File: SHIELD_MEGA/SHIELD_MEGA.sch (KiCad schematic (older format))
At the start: 2 parts

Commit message: Updating main sheet
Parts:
- added C1, C2, C3, C4: 100n, symbol Device:C
- gave numbers to parts that had none: 2
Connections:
- net +3V3: now also C1.1, C2.1
- net +5V: now also C3.1, C4.1
- net GND: now also C1.2, C2.2, C3.2, C4.2
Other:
- moved on the sheet: J1
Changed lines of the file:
@@
 $Descr A4 11693 8268
 encoding utf-8
-Sheet 1 9
-Title ""
-Date ""
-Rev ""
-Comp ""
+Sheet 1 10
+Title "SHIELD ARDUINO MEGA"
+Date "2021-11-21"
+Rev "V1"
+Comp "PROEX - UNIFEI"
 Comment1 ""
 Comment2 ""
 Comment3 ""
-Comment4 ""
+Comment4 "LINCOLN WALLACE VELOSO ALMEIDA"
 $EndDescr
 $Comp
-L Connector:Conn_01x03_Male J?
+L Connector:Conn_01x03_Male J2
 U 1 1 61954CC1
 P 9750 5950
-F 0 "J?" H 9800 6200 50  0000 C CNN
+F 0 "J2" H 9800 6200 50  0000 C CNN
 F 1 "Conn_01x03_Male" V 9700 5950 50  0000 C CNN
 F 2 "" H 9750 5950 50  0001 C CNN
@@
 $EndComp
 $Comp
-L power:+3.3V #PWR?
+L power:+3.3V #PWR01
 U 1 1 6195629E
 P 10050 5850
-F 0 "#PWR?" H 10050 5700 50  0001 C CNN
+F 0 "#PWR01" H 10050 5700 50  0001 C CNN
 F 1 "+3.3V" V 10065 5978 50  0000 L CNN
 F 2 "" H 10050 5850 50  0001 C CNN
@@
 $EndComp
 $Comp
-L power:+5V #PWR?
+L power:+5V #PWR03
 U 1 1 61956DDE
 P 10700 5950
-F 0 "#PWR?" H 10700 5800 50  0001 C CNN
+F 0 "#PWR03" H 10700 5800 50  0001 C CNN
 F 1 "+5V" V 10715 6078 50  0000 L CNN
 F 2 "" H 10700 5950 50  0001 C CNN
@@
 $EndComp
 $Comp
-L power:GND #PWR?
+L power:GND #PWR02
 U 1 1 6195741C
 P 10050 6050
-F 0 "#PWR?" H 10050 5800 50  0001 C CNN
+F 0 "#PWR02" H 10050 5800 50  0001 C CNN
 F 1 "GND" V 10055 5922 50  0000 R CNN
 F 2 "" H 10050 6050 50  0001 C CNN
@@
 Wire Wire Line
 	3400 2450 3300 2450
-Text HLabel 8300 1250 2    50   Input ~ 0
-GND
 $Sheet
 S 8300 1050 1200 1600
@@
 F0 "ESCs" 50
 F1 "ESC_PWMs.sch" 50
-$EndSheet
-Text HLabel 8300 1400 2    50   Input ~ 0
-D04
-Text HLabel 8300 1550 2    50   Input ~ 0
-D05
-Text HLabel 8300 1700 2    50   Input ~ 0
-D06
-Text HLabel 8300 1850 2    50   Input ~ 0
-D07
+F2 "GND" I L 8300 1250 50
+F3 "D04" I L 8300 1400 50
+F4 "D05" I L 8300 1550 50
+F5 "D06" I L 8300 1700 50
+F6 "D07" I L 8300 1850 50
+$EndSheet
 Wire Wire Line
 	3300 2600 4100 2600
@@
 F0 "GPS" 50
 F1 "gps_module.sch" 50
-$EndSheet
-Text HLabel 8300 3050 2    50   Input ~ 0
-GND
+F2 "GND" I L 8300 3050 50
+F3 "RX" I L 8300 3200 50
+F4 "TX" I L 8300 3350 50
+F5 "5V" I L 8300 3500 50
+$EndSheet
 Text Label 8000 3050 0    50   ~ 0
 GND
 Wire Wire Line
 	8000 3050 8300 3050
-Text HLabel 8300 3500 2    50   Input ~ 0
-5V
-Text HLabel 8300 3200 2    50   Input ~ 0
-RX
-Text HLabel 8300 3350 2    50   Input ~ 0
-TX
 Text Label 8000 3500 0    50   ~ 0
 5V
@@
 VIN
 $Comp
-L Connector:Conn_01x02_Male J?
+L Connector:Conn_01x02_Male J1
 U 1 1 61A80B16
-P 9750 5300
-F 0 "J?" H 9858 5481 50  0000 C CNN
-F 1 "Conn_01x02_Male" H 9858 5390 50  0000 C CNN
-F 2 "" H 9750 5300 50  0001 C CNN
-F 3 "~" H 9750 5300 50  0001 C CNN
-	1    9750 5300
-	1    0    0    -1
-$EndComp
-Text Label 10250 5300 0    50   ~ 0
+P 9700 5400
+F 0 "J1" H 9808 5581 50  0000 C CNN
+F 1 "Conn_01x02_Male" H 9808 5490 50  0000 C CNN
+F 2 "" H 9700 5400 50  0001 C CNN
+F 3 "~" H 9700 5400 50  0001 C CNN
+	1    9700 5400
+	1    0    0    -1
+$EndComp
+Text Label 10200 5400 0    50   ~ 0
 VIN
 Wire Wire Line
-	10250 5300 9950 5300
-Wire Wire Line
-	9950 5400 10250 5400
-Text Label 10250 5400 0    50   ~ 0
+	10200 5400 9900 5400
+Wire Wire Line
+	9900 5500 10200 5500
+Text Label 10200 5500 0    50   ~ 0
 GND
 $Sheet
@@
 F5 "VIN" I L 4100 1500 50
 F6 "~RST" I L 4100 1600 50
-F7 "SCL" I L 4100 2600 50
-F8 "SDA" I L 4100 2750 50
+F7 "SCL_ACCEL" I L 4100 2600 50
+F8 "SDA_ACCEL" I L 4100 2750 50
 F9 "D53" I L 4100 4300 50
 F10 "D52" I L 4100 4400 50
@@
 F19 "RX" I R 7550 3200 50
 F20 "TX" I R 7550 3350 50
+F21 "SCL_BAR" I R 7550 4400 50
+F22 "SDA_BAR" I R 7550 4500 50
 $EndSheet
 $Sheet
@@
 F9 "D11" I R 3300 4800 50
 $EndSheet
+$Sheet
+S 8300 4050 1000 750
+U 61BDF06A
+F0 "BAROMETRO" 50
+F1 "BAR.sch" 50
+F2 "3.3V" I L 8300 4200 50
+F3 "GND" I L 8300 4300 50
+F4 "SCL" I L 8300 4400 50
+F5 "SDA" I L 8300 4500 50
+$EndSheet
+Text Label 8100 4200 0    50   ~ 0
+3.3V
+Wire Wire Line
+	8100 4200 8300 4200
+Wire Wire Line
+	8300 4300 8100 4300
+Text Label 8100 4300 0    50   ~ 0
+GND
+Wire Wire Line
+	7550 4400 8300 4400
+Wire Wire Line
+	8300 4500 7550 4500
+$Comp
+L Device:C C3
+U 1 1 619ADA37
+P 2600 1150
+F 0 "C3" H 2715 1196 50  0000 L CNN
+F 1 "100n" H 2715 1105 50  0000 L CNN
+F 2 "" H 2638 1000 50  0001 C CNN
+F 3 "~" H 2600 1150 50  0001 C CNN
+	1    2600 1150
+	1    0    0    -1
+$EndComp
+$Comp
+L Device:C C4
+U 1 1 619AEAF2
+P 3050 1150
+F 0 "C4" H 3165 1196 50  0000 L CNN
+F 1 "100n" H 3165 1105 50  0000 L CNN
+F 2 "" H 3088 1000 50  0001 C CNN
+F 3 "~" H 3050 1150 50  0001 C CNN
+	1    3050 1150
+	1    0    0    -1
+$EndComp
+Text Label 2300 1000 0    50   ~ 0
+5V
+Wire Wire Line
+	2300 1000 2600 1000
+Wire Wire Line
+	2600 1000 3050 1000
+Connection ~ 2600 1000
+Text Label 2300 1300 0    50   ~ 0
+GND
+Wire Wire Line
+	2300 1300 2600 1300
+Wire Wire Line
+	2600 1300 3050 1300
+Connection ~ 2600 1300
+$Comp
+L Device:C C1
+U 1 1 619B7A55
+P 1450 1150
+F 0 "C1" H 1565 1196 50  0000 L CNN
+F 1 "100n" H 1565 1105 50  0000 L CNN
+F 2 "" H 1488 1000 50  0001 C CNN
+F 3 "~" H 1450 1150 50  0001 C CNN
+	1    1450 1150
+	1    0    0    -1
+$EndComp
+$Comp
+L Device:C C2
+U 1 1 619B7A5B
+P 1900 1150
+F 0 "C2" H 2015 1196 50  0000 L CNN
+F 1 "100n" H 2015 1105 50  0000 L CNN
+F 2 "" H 1938 1000 50  0001 C CNN
+F 3 "~" H 1900 1150 50  0001 C CNN
+	1    1900 1150
+	1    0    0    -1
+$EndComp
+Text Label 1150 1300 0    50   ~ 0
+GND
+Wire Wire Line
+	1150 1300 1450 1300
+Wire Wire Line
+	1450 1300 1900 1300
+Connection ~ 1450 1300
+Text Label 1150 1000 0    50   ~ 0
+3.3V
+Wire Wire Line
+	1150 1000 1450 1000
+Wire Wire Line
+	1450 1000 1900 1000
+Connection ~ 1450 1000
 $EndSCHEMATC

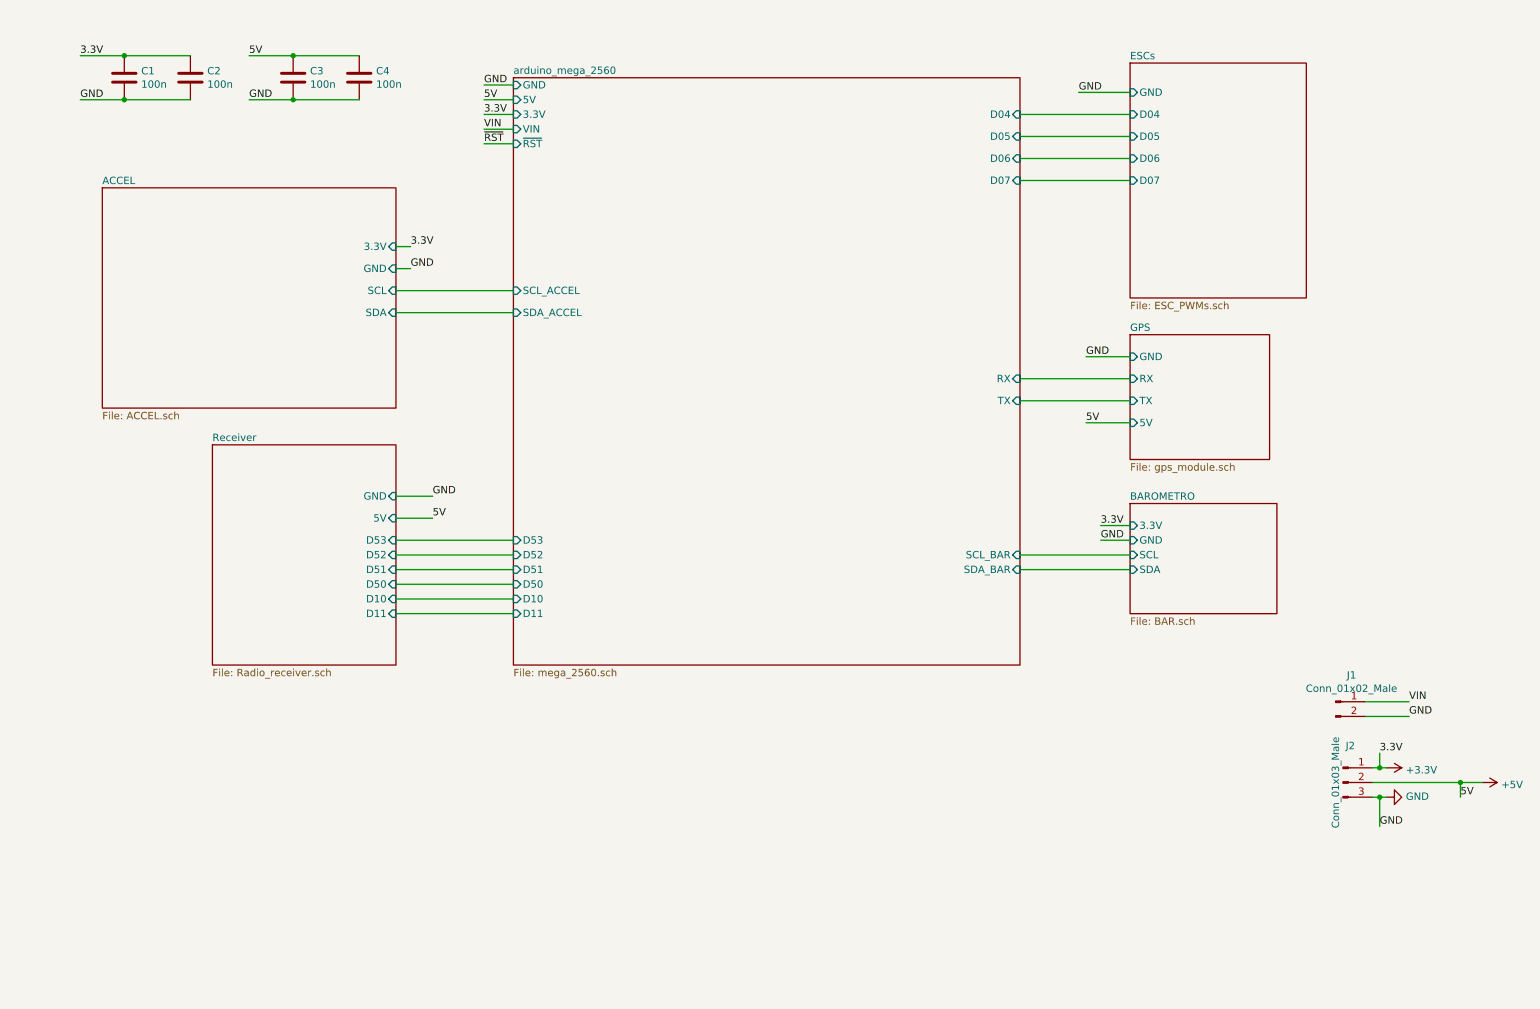
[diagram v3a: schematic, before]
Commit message: Updating references in sheet
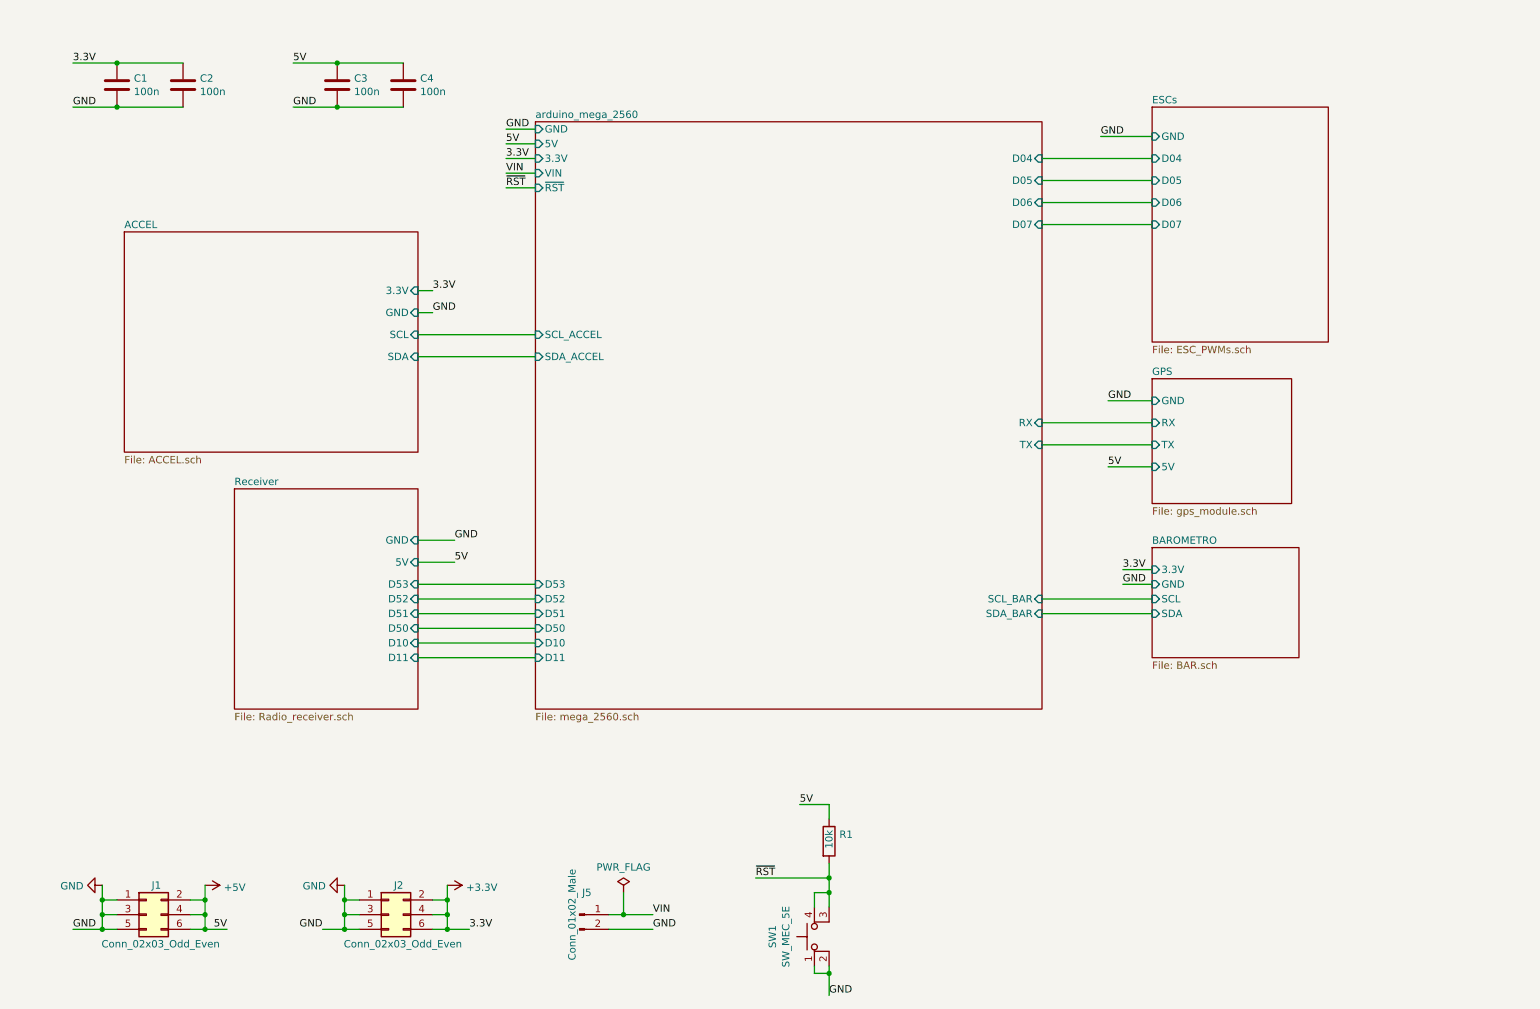
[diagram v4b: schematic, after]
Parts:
- removed J2: Conn_01x03_Male, symbol Connector:Conn_01x03_Male
- added J1, J2: Conn_02x03_Odd_Even, Connector_PinHeader_2.54mm:PinHeader_2x03_P2.54mm_Vertical, symbol Connector_Generic:Conn_02x03_Odd_Even
- added R1: 10k, Resistor_SMD:R_0805_2012Metric_Pad1.20x1.40mm_HandSolder, symbol Device:R
- added SW1: SW_MEC_5E, push_button:TE_1825910-2, symbol Switch:SW_MEC_5E
- C1, C2, C3, C4: footprint (none) -> Capacitor_SMD:C_0805_2012Metric_Pad1.18x1.45mm_HandSolder
- J5: renamed from J1; footprint (none) -> Connector_PinHeader_2.54mm:PinHeader_1x02_P2.54mm_Vertical
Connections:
- net +3V3: now also J2.2 (Pin_2), J2.4 (Pin_4), J2.6 (Pin_6)
- net +5V: now also J1.2 (Pin_2), J1.4 (Pin_4), J1.6 (Pin_6), R1.1
- net GND: now also J1.1 (Pin_1), J1.3 (Pin_3), J1.5 (Pin_5), J2.1 (Pin_1), J2.3 (Pin_3), J2.5 (Pin_5), SW1.1, SW1.2
- net ~RST: now also R1.2, SW1.3 (K), SW1.4 (A)
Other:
- moved on the sheet: C1, C2, C3, C4, J5

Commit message: Adding RGB led on main sheet
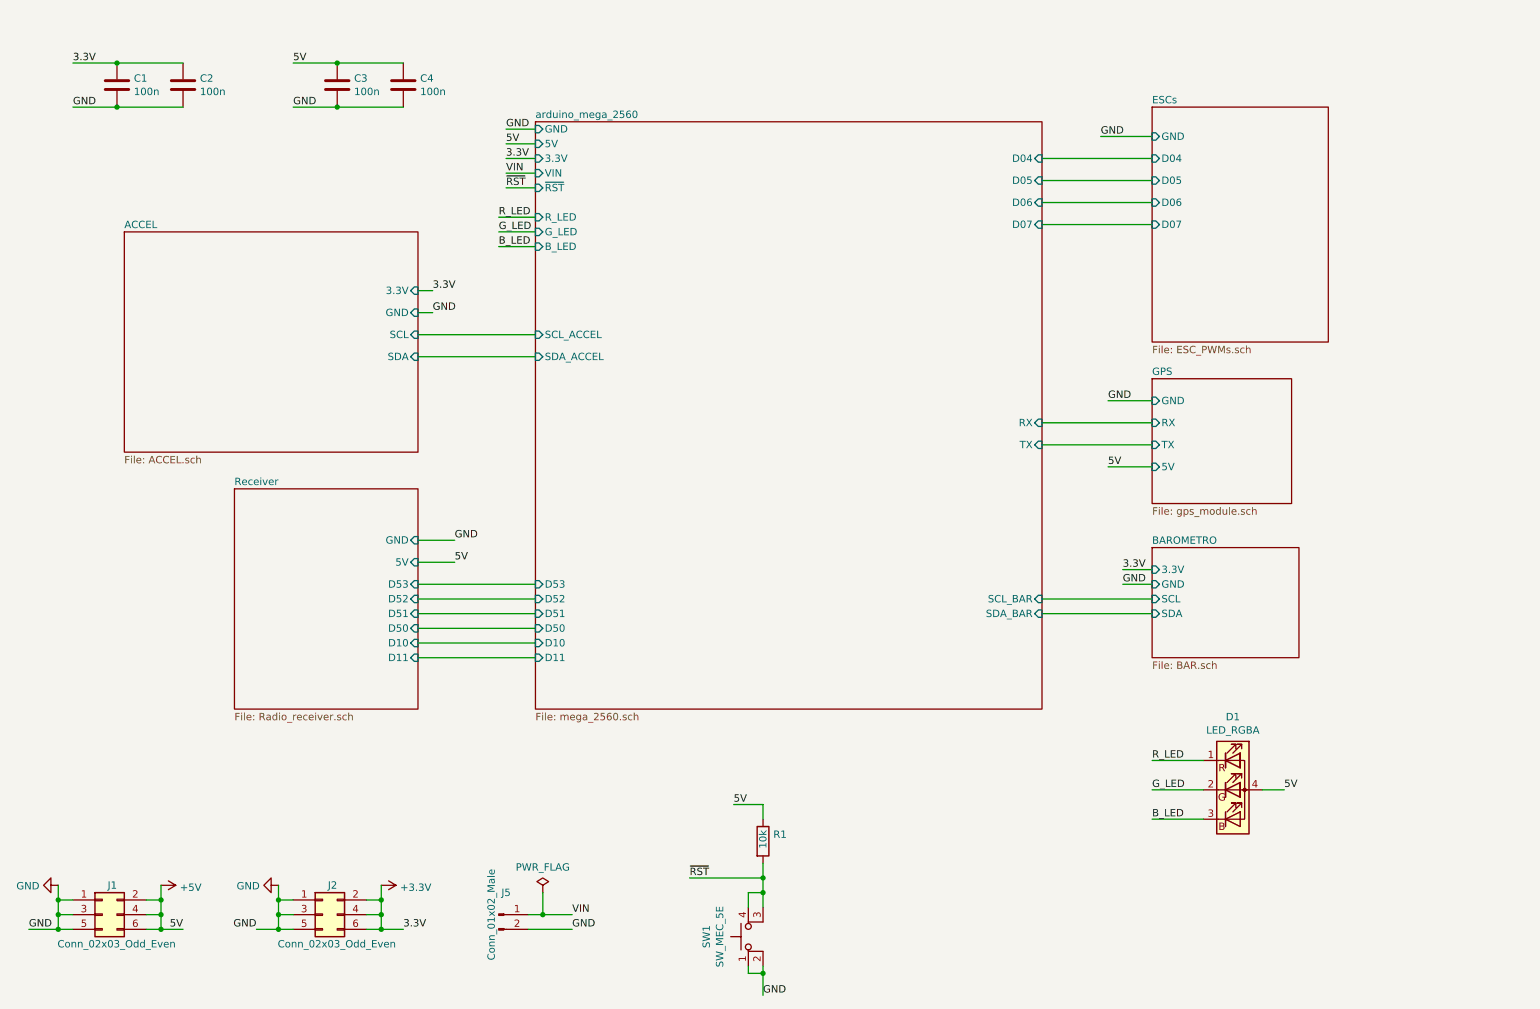
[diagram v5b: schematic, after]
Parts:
- added D1: LED_RGBA, symbol Device:LED_RGBA
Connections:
- net +5V: now also D1.4 (A)
- new net B_LED: D1.3 (BK)
- new net G_LED: D1.2 (GK)
- new net R_LED: D1.1 (RK)
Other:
- moved on the sheet: J1, J2, J5, R1, SW1
